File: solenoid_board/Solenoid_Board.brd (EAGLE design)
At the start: 22.5 x 29.5 mm, 19 parts, among them Q1 MOSFET-NCHANNELSMD, Q2 MOSFET-NCHANNELSMD, Q3 MOSFET-NCHANNELSMD, Q4 MOSFET-NCHANNELSMD

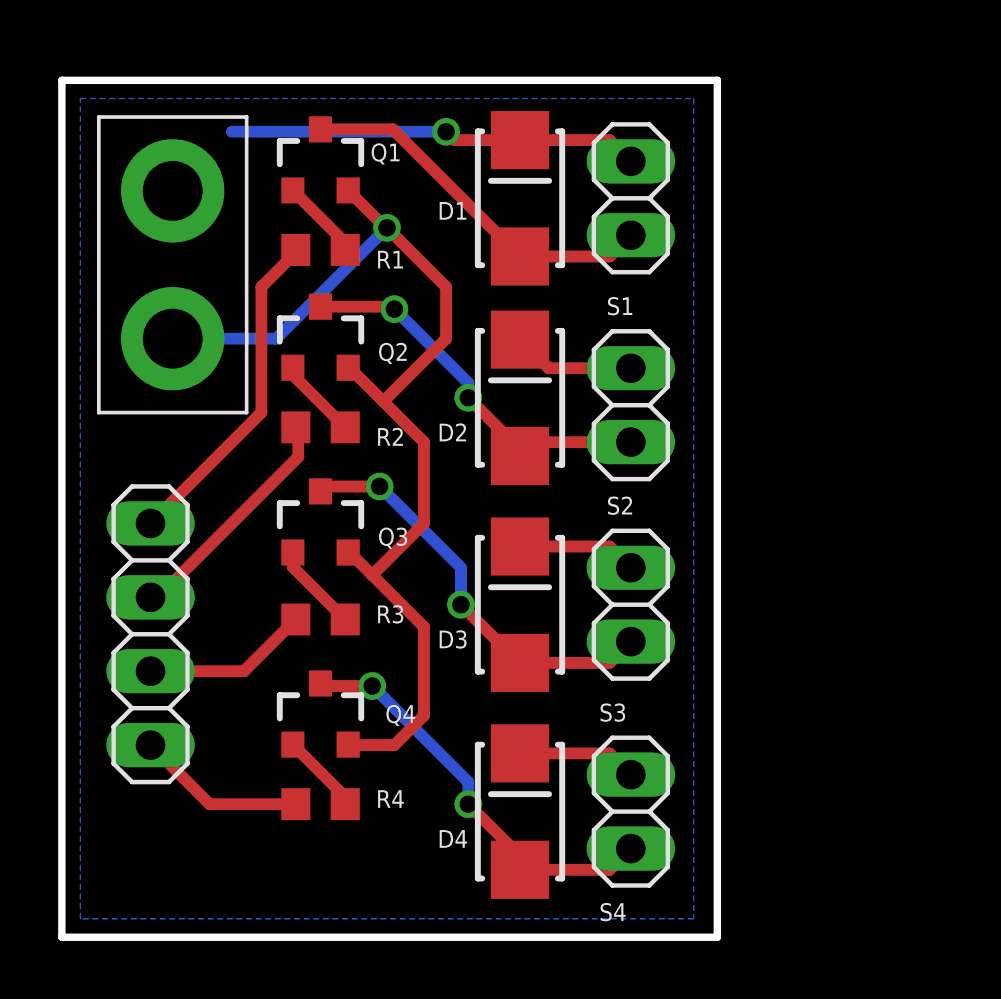
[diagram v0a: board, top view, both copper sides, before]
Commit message: Added the new connectors and finished the solenoid.
Change-Id: Ib5061dd60fbaf8b9f1d173d821b204b554eb5b3c
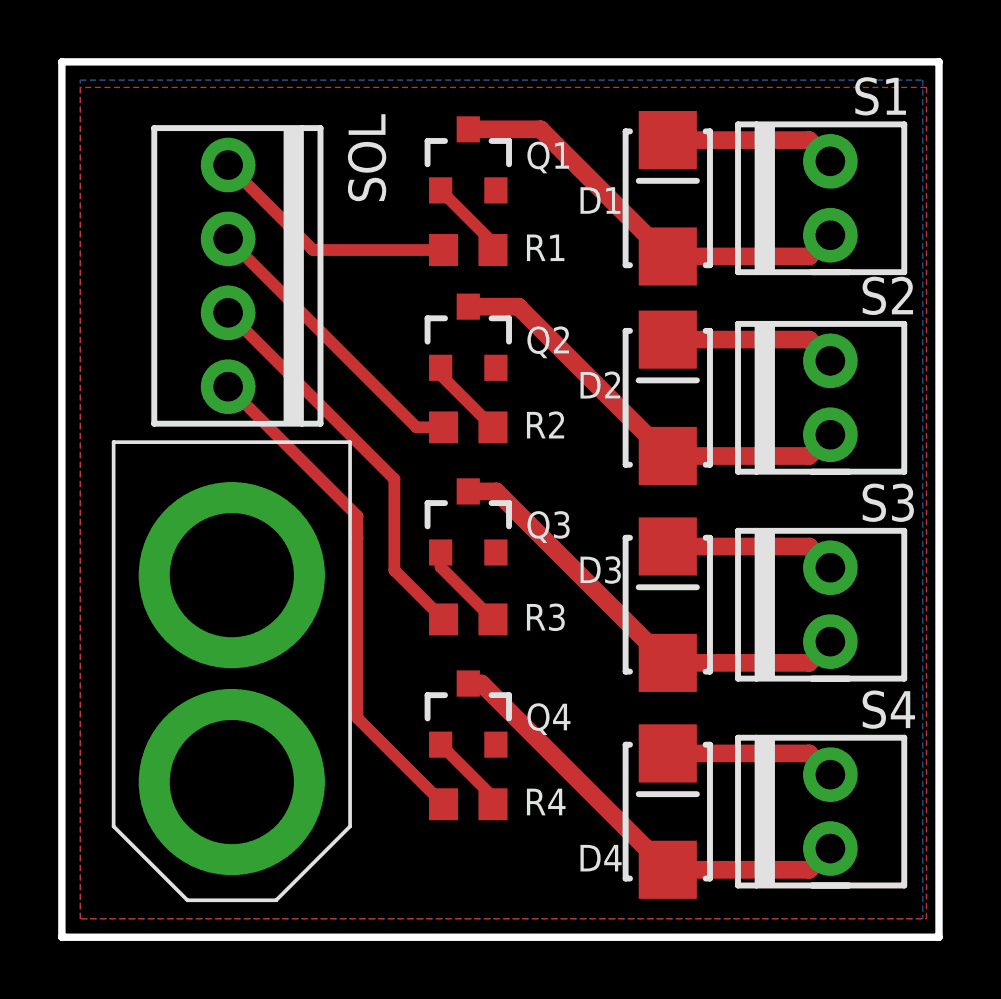
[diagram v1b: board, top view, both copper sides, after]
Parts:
- removed JP1: (no value), SparkFun:1X02_XTRA_BIG
- removed JP7: (no value), pinhead:1X04
- added SOL: (no value), pie:1X04
- added U$2: XT60CONNECTOR, pie:XT60CONNECTOR
- S1, S2, S3, S4: device pinhead:1X02 -> pie:1X02
- moved S1 6.97 mm to (26.4, 24.1), turned to 90 degrees
- moved S3 6.97 mm to (26.4, 10.2), turned to 90 degrees
- moved S4 6.97 mm to (26.4, 3.05), turned to 90 degrees
- moved S2 6.93 mm to (26.4, 17.3), turned to 90 degrees
- moved D1 5.08 mm to (20.8, 25.4)
- moved D2 5.08 mm to (20.8, 18.5)
- moved D3 5.08 mm to (20.8, 11.4)
- moved D4 5.08 mm to (20.8, 4.32)
- moved Q1 5.08 mm to (14.0, 26.7)
- moved Q2 5.08 mm to (14.0, 20.6)
- moved Q3 5.08 mm to (14.0, 14.2)
- moved Q4 5.08 mm to (14.0, 7.62)
- moved R1 5.08 mm to (14.0, 23.6)
- moved R2 5.08 mm to (14.0, 17.5)
- moved R3 5.08 mm to (14.0, 10.9)
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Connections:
- net 12V: now also S1.2, S2.2, S3.2, S4.2, U$2.12V; no longer JP1.2, S1.1, S2.1, S3.1, S4.1
- net GND: now also U$2.GND; no longer JP1.1
- net N$1: now also SOL.1; no longer JP7.1
- net N$2: now also S1.1; no longer S1.2
- net N$3: now also S4.1; no longer S4.2
- net N$4: now also S3.1; no longer S3.2
- net N$5: now also SOL.2; no longer JP7.2
- net N$6: now also SOL.3; no longer JP7.3
- net N$7: now also SOL.4; no longer JP7.4
- net N$8: now also S2.1; no longer S2.2
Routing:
- net GND: track 37.3 -> 0.05 mm, vias 1 -> 0
- net N$7: track 5.83 -> 17.4 mm
- net N$6: track 5.73 -> 13.6 mm
- net 12V: track 26.6 -> 23.6 mm, vias 1 -> 0
- net N$1: track 11.5 -> 8.70 mm
- net N$5: track 8.13 -> 10.1 mm
- net N$2: track 12.8 -> 14.6 mm
- net N$8: track 13.4 -> 14.9 mm, vias 2 -> 0
- net N$3: track 14.3 -> 15.4 mm, vias 2 -> 0
- net N$4: track 14.3 -> 15.2 mm, vias 2 -> 0
- added copper zone on layer 1, net GND
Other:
- board size 22.5 x 29.5 mm -> 30.1 x 30.1 mm
- board text added: "2012.11.19"
- board text added: "PiE Solenoid Board v1.5"
- board text added: "Revision B"
- board text removed: "1/11/12"
- board text removed: "PiE Solenoid Board v1.0"
- board text removed: "Rev.A"
